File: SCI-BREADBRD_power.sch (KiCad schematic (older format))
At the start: 3 parts

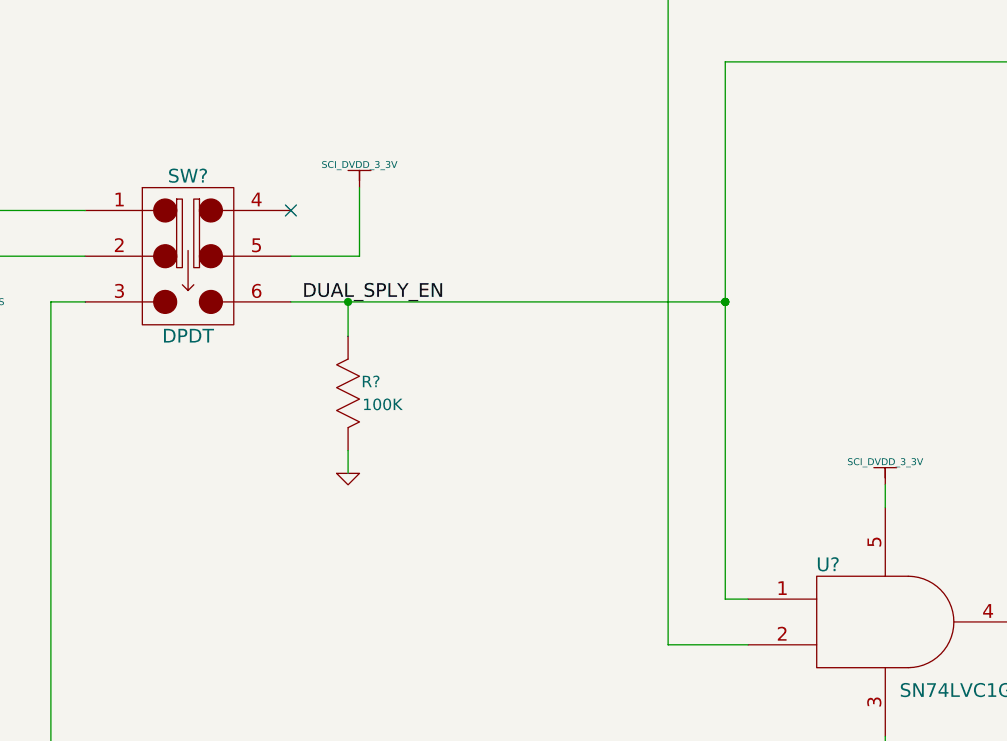
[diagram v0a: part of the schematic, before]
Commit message: Fixed the footprint properties of various parts throughout the schematic to make sure they are all point to valid footprints.
Added SCI-BREADBRD.cmp to specify which footprints should be used for
each part.

Added netlists to the .gitignore as those can be generated easily in
eeschema.
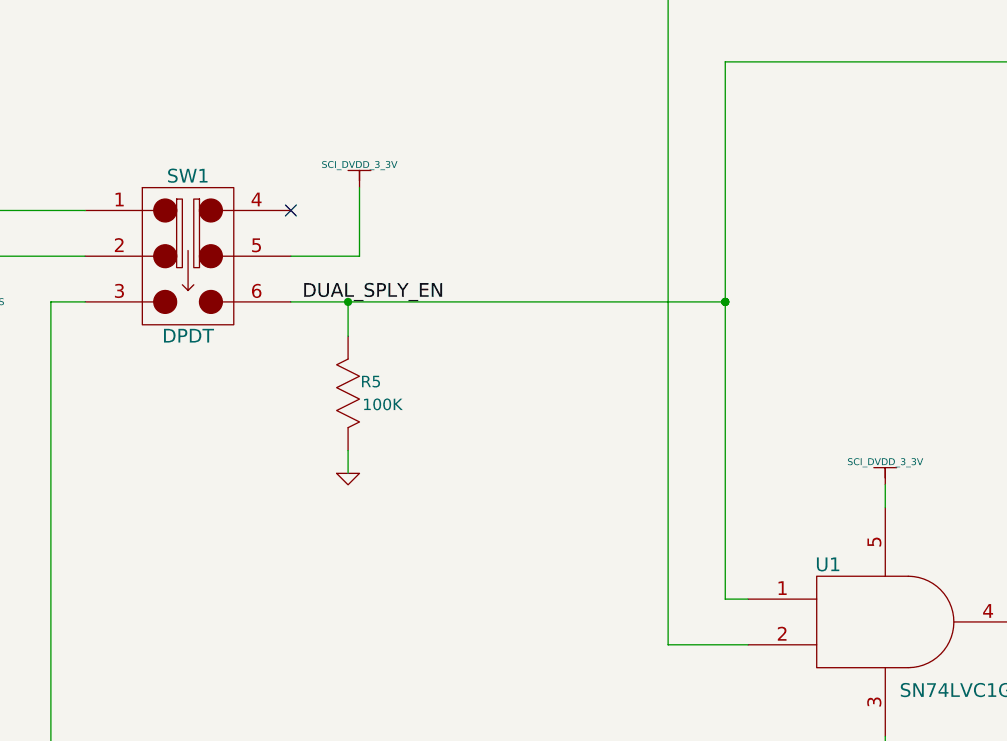
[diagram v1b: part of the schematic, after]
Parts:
- R5: renamed from R?; footprint SM0402 -> 0402
- gave numbers to parts that had none: 2
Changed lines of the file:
@@
-EESchema Schematic File Version 2  date Fri 27 Apr 2012 04:22:34 AM EDT
+EESchema Schematic File Version 2  date Fri 27 Apr 2012 08:55:37 AM EDT
 LIBS:custom_transistors
 LIBS:TI_custom
@@
 $EndDescr
 $Comp
-L DPDT SW?
+L DPDT SW1
 U 1 1 4F8CA839
 P 2900 3400
-F 0 "SW?" H 2900 3750 60  0000 C CNN
+F 0 "SW1" H 2900 3750 60  0000 C CNN
 F 1 "DPDT" H 2900 3050 60  0000 C CNN
 F 2 "CK_DPDT_SMT" H 2900 3400 60  0001 C CNN
@@
 $EndComp
 $Comp
-L SN74LVC1G08DCK U?
+L SN74LVC1G08DCK U1
 U 1 1 4F8CA848
 P 5950 5000
-F 0 "U?" H 5700 5250 60  0000 C CNN
+F 0 "U1" H 5700 5250 60  0000 C CNN
 F 1 "SN74LVC1G08DBV" H 6400 4700 60  0000 C CNN
 F 2 "SOP_5_DBV" H 5950 5000 60  0001 C CNN
@@
 $EndComp
 $Comp
-L AFE/SCI_ANLG_VSS #PWR?
+L AFE/SCI_ANLG_VSS #PWR040
 U 1 1 4F9A14F6
 P 1900 3500
-F 0 "#PWR?" H 1900 3400 30  0001 C CNN
+F 0 "#PWR040" H 1900 3400 30  0001 C CNN
 F 1 "AFE/SCI_ANLG_VSS" H 1900 3400 30  0000 C CNN
 	1    1900 3500
@@
 $EndComp
 $Comp
-L GND #PWR?
+L GND #PWR041
 U 1 1 4F9A1627
 P 1750 3350
-F 0 "#PWR?" H 1750 3350 30  0001 C CNN
+F 0 "#PWR041" H 1750 3350 30  0001 C CNN
 F 1 "GND" H 1750 3280 30  0001 C CNN
 	1    1750 3350
@@
 $EndComp
 $Comp
-L SCI_DVDD_3_3V #PWR?
+L SCI_DVDD_3_3V #PWR042
 U 1 1 4F9A18A3
 P 3650 3100
-F 0 "#PWR?" H 3650 3200 30  0001 C CNN
+F 0 "#PWR042" H 3650 3200 30  0001 C CNN
 F 1 "SCI_DVDD_3_3V" H 3650 3200 30  0000 C CNN
 	1    3650 3100
@@
 DUAL_SPLY_EN
 $Comp
-L SCI_DVDD_3_3V #PWR?
+L SCI_DVDD_3_3V #PWR043
 U 1 1 4F9A1DFD
 P 5950 4400
-F 0 "#PWR?" H 5950 4500 30  0001 C CNN
+F 0 "#PWR043" H 5950 4500 30  0001 C CNN
 F 1 "SCI_DVDD_3_3V" H 5950 4500 30  0000 C CNN
 	1    5950 4400
@@
 $EndComp
 $Comp
-L GND #PWR?
+L GND #PWR044
 U 1 1 4F9A1F73
 P 5950 5600
-F 0 "#PWR?" H 5950 5600 30  0001 C CNN
+F 0 "#PWR044" H 5950 5600 30  0001 C CNN
 F 1 "GND" H 5950 5530 30  0001 C CNN
 	1    5950 5600
@@
 ANLG_PWR_EN
 $Comp
-L R_US R?
+L R_US R5
 U 1 1 4F9A4A29
 P 3600 4000
-F 0 "R?" V 3650 3900 50  0000 C CNN
+F 0 "R5" V 3650 3900 50  0000 C CNN
 F 1 "100K" V 3550 3850 50  0000 C CNN
-F 2 "SM0402" H 3600 4000 60  0001 C CNN
+F 2 "0402" H 3600 4000 60  0001 C CNN
 F 4 "Panasonic - ECG" H 3600 4000 60  0001 C CNN "Manufacturer"
 F 5 "ERJ-2GEJ104X" H 3600 4000 60  0001 C CNN "Part Number"
@@
 $EndComp
 $Comp
-L GND #PWR?
+L GND #PWR045
 U 1 1 4F9A4A85
 P 3600 4350
-F 0 "#PWR?" H 3600 4350 30  0001 C CNN
+F 0 "#PWR045" H 3600 4350 30  0001 C CNN
 F 1 "GND" H 3600 4280 30  0001 C CNN
 	1    3600 4350
